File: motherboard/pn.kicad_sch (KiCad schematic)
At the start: 82 parts, among them J201 BNC, J202 Conn_01x05, J203 BNC, Q201 2N7002, Q202 2N7002, Q203 2N7002, U201 LMH6609, U202 SYPD-1, U203 LM393, U204 AD797AR, U205 LM393, U206 OPA192IDR

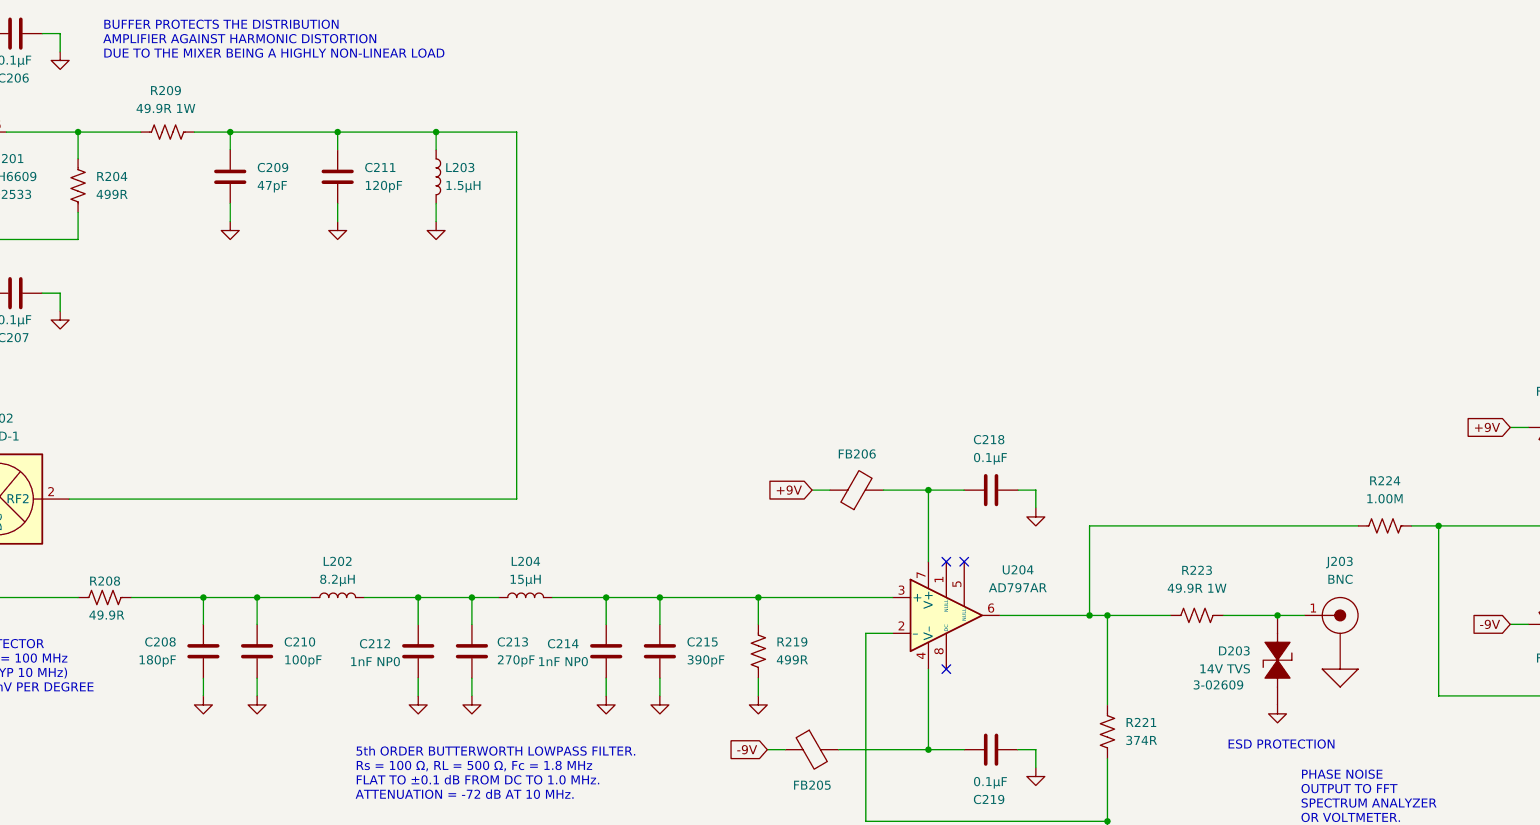
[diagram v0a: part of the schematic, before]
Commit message: make FREQ_CTL filter cap an NP0 part
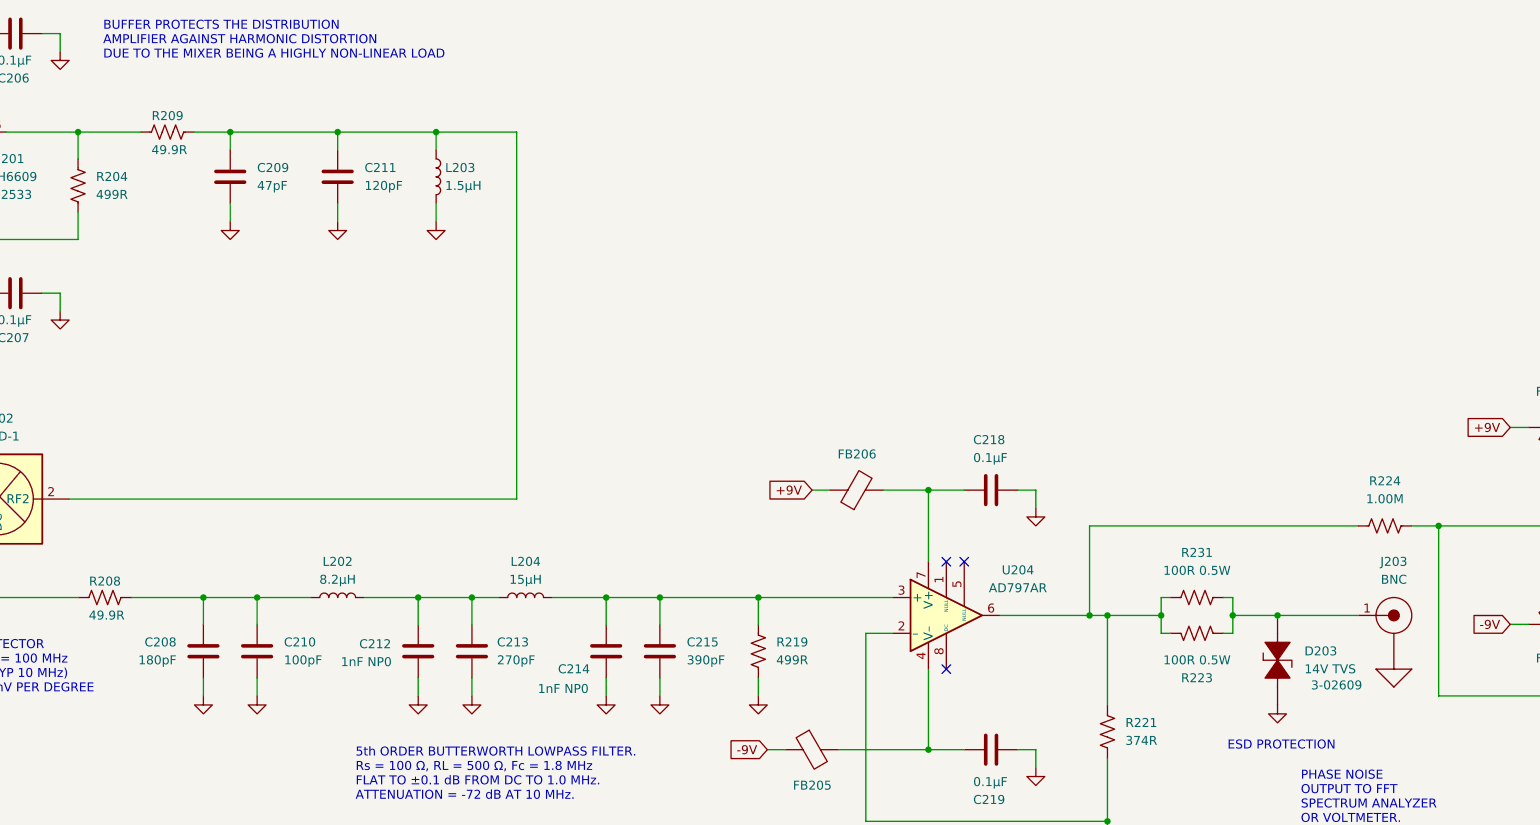
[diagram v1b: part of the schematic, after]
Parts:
- removed R209, R223: 49.9R 1W, Resistor_SMD:R_2512_6332Metric, symbol #SRS:4_Resistors/4-02510
- added R209: 49.9R, Resistor_SMD:R_0603_1608Metric, symbol #SRS:4_Resistors/4-02032
- added R223, R231: 100R 0.5W, Resistor_SMD:R_1206_3216Metric, symbol #SRS:4_Resistors/4-02555
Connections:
- net at R204.1, U201.6: now also R209.1
- net at C209.1, C211.1, L203.1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: now also R209.2
- net at R221.1, R224.1, U204.6: now also R223.1, R231.1
- net at D203.1 (CATHODE), J203.1 (C): now also R223.2, R231.2
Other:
- moved on the sheet: D203, J203

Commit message: replace mosfet with analog switch
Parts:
- removed C203: 10μF, Capacitor_SMD:C_0805_2012Metric, symbol #SRS:5_Capacitors/5-00954
- removed J202: Conn_01x05, Connector_PinHeader_2.54mm:PinHeader_1x05_P2.54mm_Vertical, symbol Connector_Generic:Conn_01x05
- removed Q201, Q202: 2N7002, Package_TO_SOT_SMD:SOT-23, symbol Transistor_FET:2N7002
- removed R210, R213: 1.00K, Resistor_SMD:R_0603_1608Metric, symbol #SRS:4_Resistors/4-02157
- removed R211, R212: 4.99K, Resistor_SMD:R_0603_1608Metric, symbol #SRS:4_Resistors/4-02224
- added C203: 0.1μF C0G, Capacitor_SMD:C_1206_3216Metric, symbol #SRS:5_Capacitors/5-01075
- added C225: 1nF NP0, Capacitor_SMD:C_0603_1608Metric, symbol #SRS:5_Capacitors/5-00740
- added R210: 10.0K, Resistor_SMD:R_0603_1608Metric, symbol #SRS:4_Resistors/4-02253
- added R211: 1.00K, Resistor_SMD:R_0603_1608Metric, symbol #SRS:4_Resistors/4-02157
- added U207: DG419DY, Package_SO:SO-8_3.9x4.9mm_P1.27mm, symbol #SRS:3_ICs/3-01367
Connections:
- net +5V: now also R201.2, U207.5 (VL)
- net +9V: now also U207.4 (V+)
- net -9V: now also U207.7 (V-)
- net FREQ_CTL: now also C225.1, R211.2, U207.1; no longer U206.6
- net GND: now also C203.2, R210.1, U207.3 (GND); no longer U206.3 (+)
- net LOCKED: no longer R201.1
- net ~{SIG_PRESENT}: now also U207.6
- net at C223.1, R224.2, R228.2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: now also U207.8
- new net: C203.1, R201.1, R210.2, U206.3 (+)
- new net: C225.2, R211.1, U206.6
- no-connect marks 3 -> 4
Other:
- note removed: "FRONT PANEL LEDs"
- note removed: "MATES TO LED BOARD 7-01993 WITH GREEN/GREEN/GREEN/RED LEDS INSTALLED, VIA SHORT 5 POS RIBBON CABLE (1-01043)"

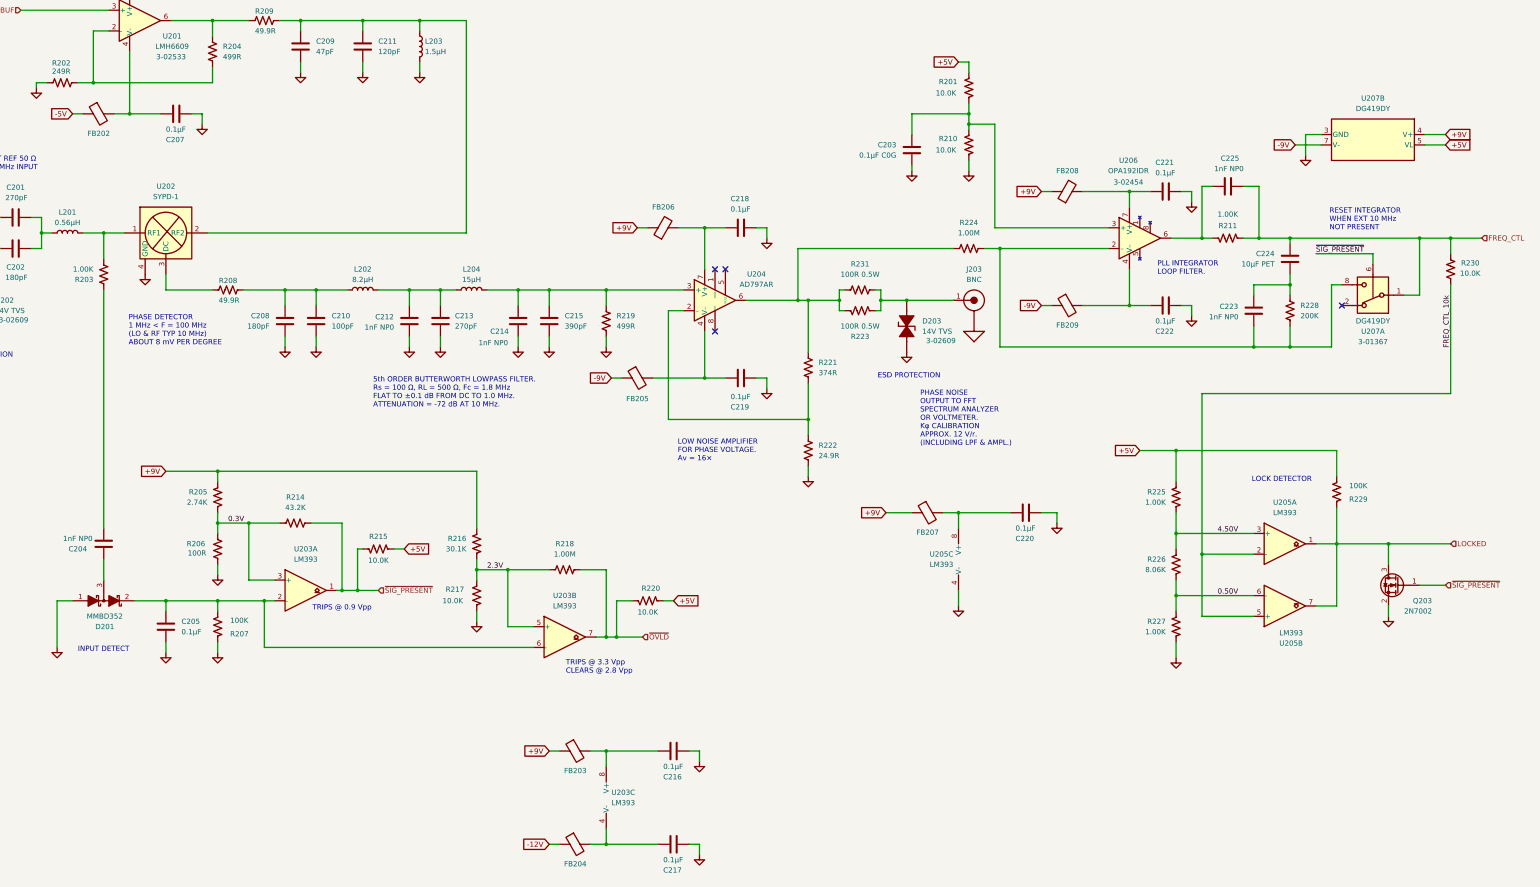
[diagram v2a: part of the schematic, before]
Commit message: better comparators for ~FAULT
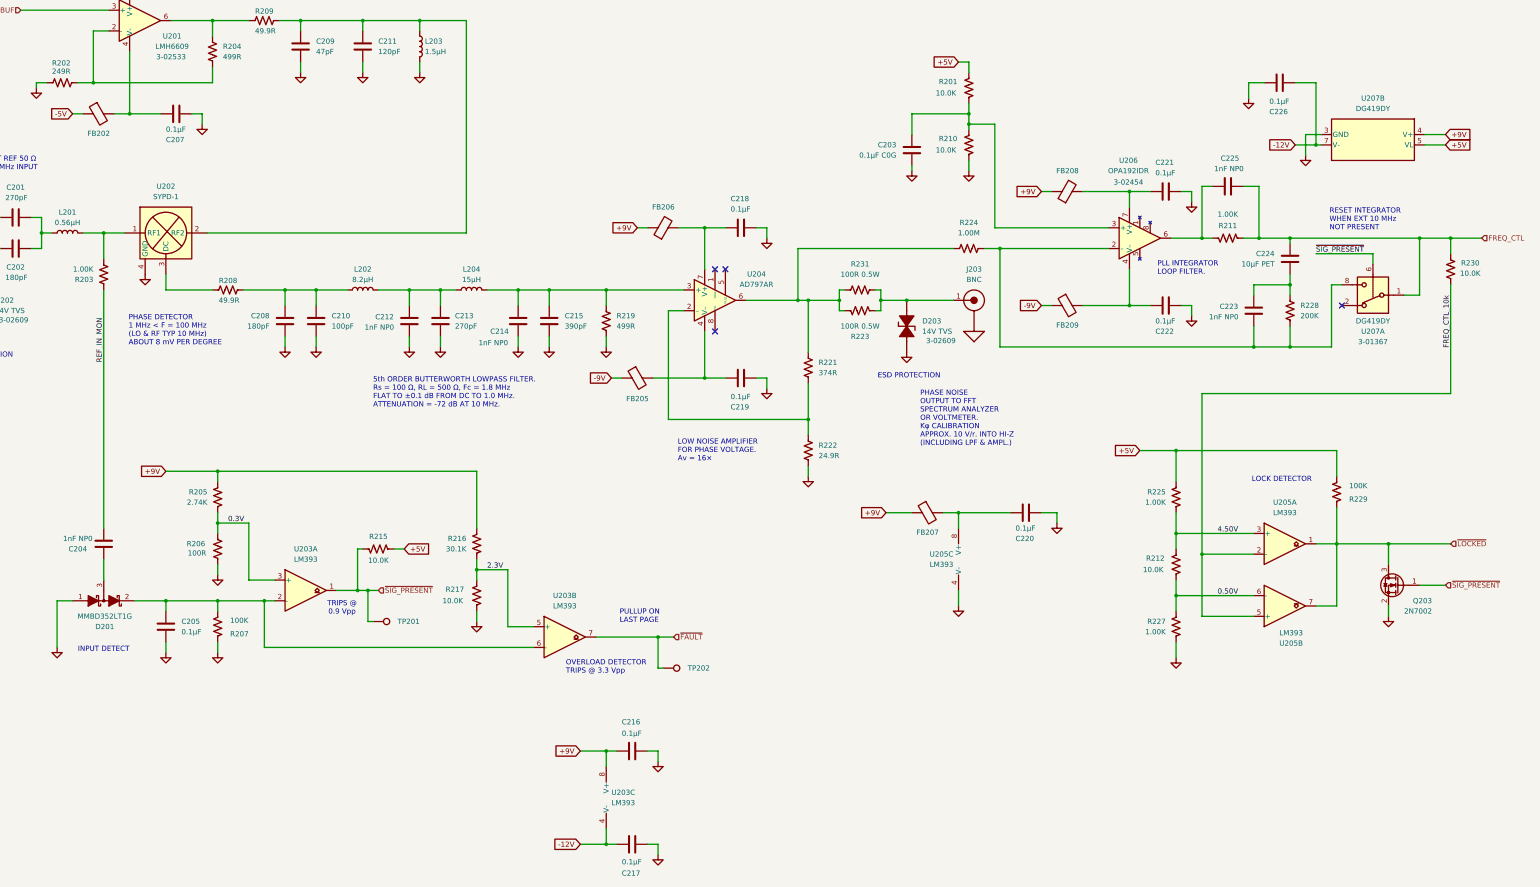
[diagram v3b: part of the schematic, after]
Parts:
- removed FB203, FB204: 742863160, Inductor_SMD:L_0603_1608Metric, symbol #SRS:6_Other/6-01093
- removed R214: 43.2K, Resistor_SMD:R_0603_1608Metric, symbol #SRS:4_Resistors/4-02314
- removed R218: 1.00M, Resistor_SMD:R_0603_1608Metric, symbol #SRS:4_Resistors/4-02445
- removed R220: 10.0K, Resistor_SMD:R_0603_1608Metric, symbol #SRS:4_Resistors/4-02253
- removed R226: 8.06K, Resistor_SMD:R_0603_1608Metric, symbol #SRS:4_Resistors/4-02244
- added C226: 0.1μF, Capacitor_SMD:C_0603_1608Metric, symbol #SRS:5_Capacitors/5-00764
- added R212: 10.0K, Resistor_SMD:R_0603_1608Metric, symbol #SRS:4_Resistors/4-02253
- added TP201, TP202: TestPoint, TestPoint:TestPoint_THTPad_D1.0mm_Drill0.5mm, symbol Connector:TestPoint
- D201: value MMBD352 -> MMBD352LT1G
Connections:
- net +9V: now also C216.2, U203.8 (V+)
- net -12V: now also C217.2, U203.4 (V-), U207.7 (V-), C226.1
- net -9V: no longer U207.7 (V-)
- net 0.50V: now also R212.1
- net 4.50V: now also R212.2
- net GND: now also C226.2
- net ~{SIG_PRESENT}: now also TP201.1
- net REF_IN_MON: now reaches C204.1, R203.2
- net LOCKED renamed ~{LOCKED}
- net ~{OVLD} renamed ~{FAULT}
- net ~{FAULT}: now also TP202.1
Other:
- note added: "OVERLOAD DETECTOR TRIPS @ 3.3 Vpp"
- note added: "PHASE NOISE OUTPUT TO FFT SPECTRUM ANALYZER OR VOLTMETER. Kφ CALIBRATION APPROX. 10 V/r. INTO HI-Z (INCLUDING LPF & AMPL.)"
- note added: "PULLUP ON LAST PAGE"
- note removed: "PHASE NOISE OUTPUT TO FFT SPECTRUM ANALYZER OR VOLTMETER. Kφ CALIBRATION APPROX. 12 V/r. (INCLUDING LPF & AMPL.)"
- note removed: "TRIPS @ 3.3 Vpp CLEARS @ 2.8 Vpp"
